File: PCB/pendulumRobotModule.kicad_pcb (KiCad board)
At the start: 2 copper layers, 33 x 100 mm, 26 parts, among them J1 Conn_01x02_Female, J2 conn_3x4, J3 Conn_01x02_Male, J4 Conn_01x04_Female, J5 conn_3x3, J7 Conn_01x04_Female, U1 ESP32-devKit, U2 MPU6050-breakout, U3 buckConverter-adj

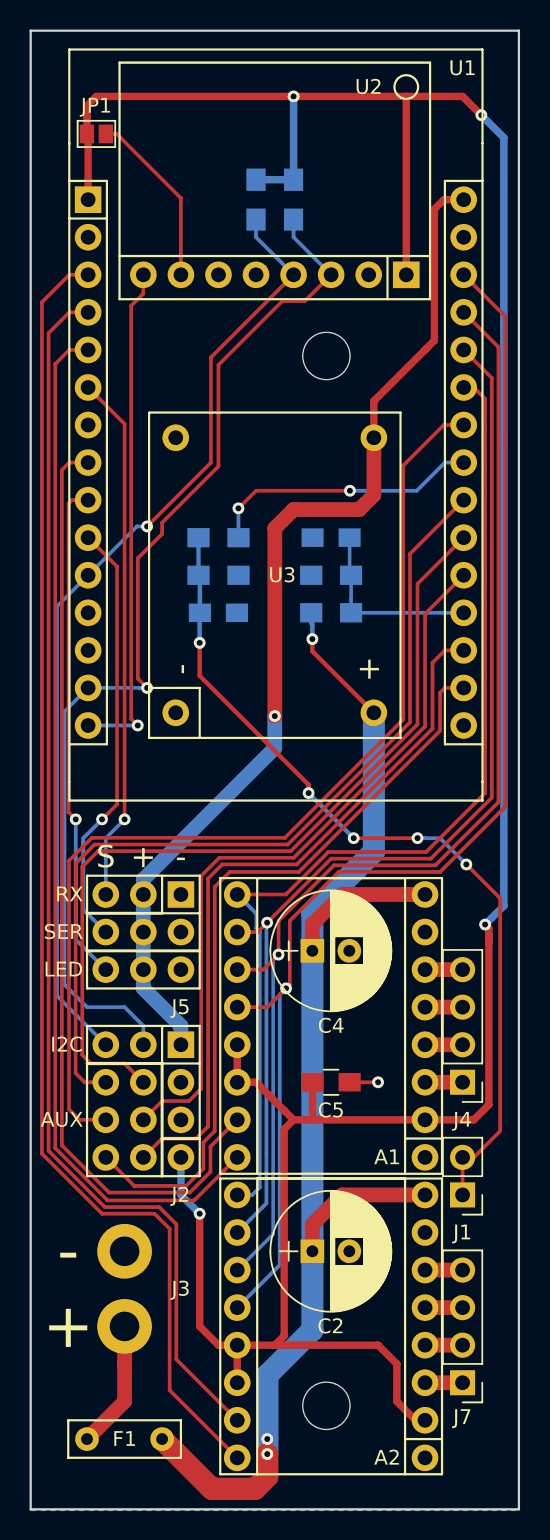
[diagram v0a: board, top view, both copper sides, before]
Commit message: PCB updates: increased 24V trace thickness, added a via (or rather added trace to via) in that signal, and added stepper motor enable pull-up to 3V3.
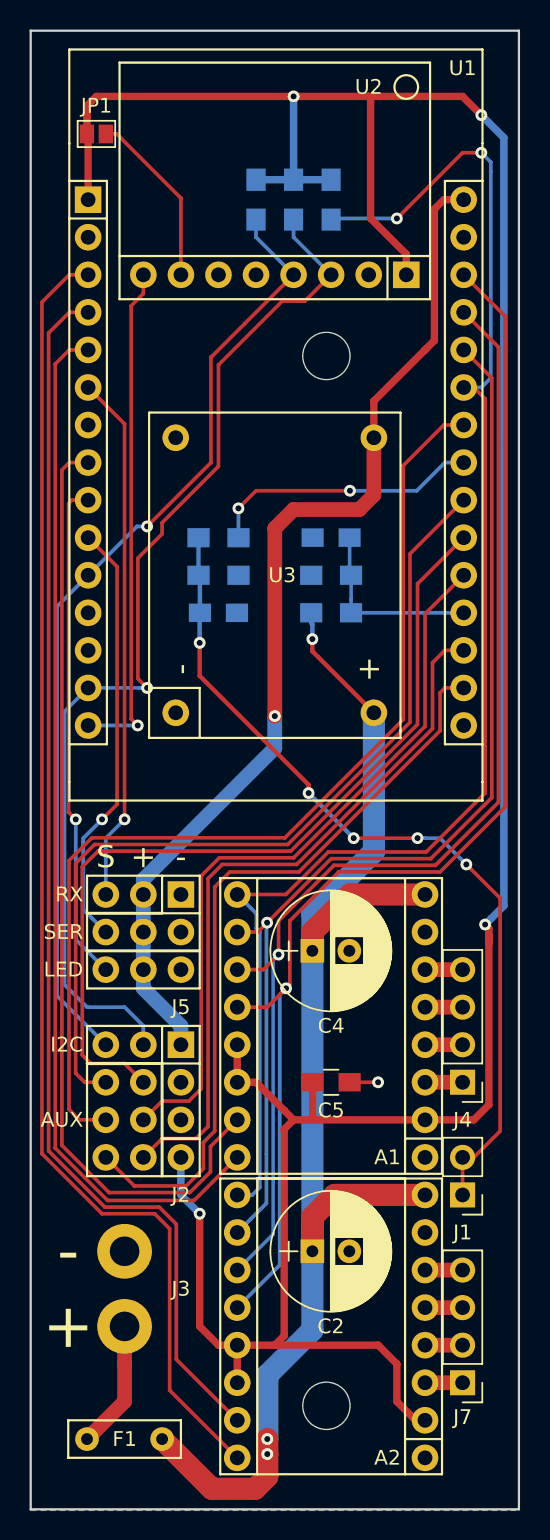
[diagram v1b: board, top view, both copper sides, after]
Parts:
- added R7: 10k, Resistors_SMD:R_0805_HandSoldering, B.Cu at (111.8, 44.5)
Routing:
- net /motEn: track 70.2 -> 99.8 mm, vias 0 -> 2
- net VCC: track 196.1 -> 199.6 mm
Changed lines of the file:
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@@
     (thickness 1.6)
     (drawings 21)
-    (tracks 368)
+    (tracks 383)
     (zones 0)
-    (modules 26)
+    (modules 27)
     (nets 44)
   )
@@
     (tags "resistor 0805")
     (attr smd)
-    (fp_text reference R3 (at 0 2.54) (layer B.SilkS)
+    (fp_text reference R3 (at 3.175 0) (layer B.SilkS)
       (effects (font (size 1 1) (thickness 0.15)) (justify mirror))
     )
@@
     (tags "resistor 0805")
     (attr smd)
-    (fp_text reference R4 (at 0 -2.54) (layer B.SilkS)
+    (fp_text reference R4 (at 3.175 0) (layer B.SilkS)
       (effects (font (size 1 1) (thickness 0.15)) (justify mirror))
     )
@@
     )
   )
+  (module Resistors_SMD:R_0805_HandSoldering (layer B.Cu)
+    (at 111.76 44.45 270)
+    (descr "Resistor SMD 0805, hand soldering")
+    (tags "resistor 0805")
+    (attr smd)
+    (fp_text reference R7 (at -3.175 0 180) (layer B.SilkS)
+      (effects (font (size 1 1) (thickness 0.15)) (justify mirror))
+    )
+    (fp_text value 10k (at 0 -1.75 270) (layer B.Fab)
+      (effects (font (size 1 1) (thickness 0.15)) (justify mirror))
+    )
+    (fp_line (start 2.35 -0.9) (end -2.35 -0.9) (layer B.CrtYd) (width 0.05))
+    (fp_line (start 2.35 -0.9) (end 2.35 0.9) (layer B.CrtYd) (width 0.05))
+    (fp_line (start -2.35 0.9) (end -2.35 -0.9) (layer B.CrtYd) (width 0.05))
+    (fp_line (start -2.35 0.9) (end 2.35 0.9) (layer B.CrtYd) (width 0.05))
+    (fp_line (start -0.6 0.88) (end 0.6 0.88) (layer B.SilkS) (width 0.12))
+    (fp_line (start 0.6 -0.88) (end -0.6 -0.88) (layer B.SilkS) (width 0.12))
+    (fp_line (start -1 0.62) (end 1 0.62) (layer B.Fab) (width 0.1))
+    (fp_line (start 1 0.62) (end 1 -0.62) (layer B.Fab) (width 0.1))
+    (fp_line (start 1 -0.62) (end -1 -0.62) (layer B.Fab) (width 0.1))
+    (fp_line (start -1 -0.62) (end -1 0.62) (layer B.Fab) (width 0.1))
+    (fp_text user %R (at 0 0 270) (layer B.Fab)
+      (effects (font (size 0.5 0.5) (thickness 0.075)) (justify mirror))
+    )
+    (pad 2 smd rect (at 1.35 0 270) (size 1.5 1.3) (layers B.Cu B.Paste B.Mask)
+      (net 33 /motEn))
+    (pad 1 smd rect (at -1.35 0 270) (size 1.5 1.3) (layers B.Cu B.Paste B.Mask)
+      (net 5 VCC))
+    (model ${KISYS3DMOD}/Resistors_SMD.3dshapes/R_0805.wrl
+      (at (xyz 0 0 0))
+      (scale (xyz 1 1 1))
+      (rotate (xyz 0 0 0))
+    )
+  )
   (gr_text "October 2018\ngitlab.com/kloppertje/PendulumRobot/\nelexperiment.nl" (at 107.696 39.37) (layer B.SilkS)
     (effects (font (size 1 1) (thickness 0.2)) (justify mirror))
@@
   (segment (start 123.19 91.694) (end 123.19 107.442) (width 0.25) (layer F.Cu) (net 2))
   (segment (start 110.49 115.57) (end 110.49 95.25) (width 1.5) (layer B.Cu) (net 3))
-  (segment (start 110.49 113.77) (end 110.49 115.57) (width 1) (layer F.Cu) (net 3))
-  (segment (start 112.5 111.76) (end 110.49 113.77) (width 1) (layer F.Cu) (net 3))
-  (segment (start 118.11 111.76) (end 112.5 111.76) (width 1) (layer F.Cu) (net 3))
   (segment (start 110.49 95.25) (end 110.49 92.71) (width 1.5) (layer B.Cu) (net 3))
   (segment (start 110.49 92.71) (end 114.65 88.55) (width 1.5) (layer B.Cu) (net 3))
   (segment (start 114.65 88.55) (end 114.65 79.15) (width 1.5) (layer B.Cu) (net 3))
-  (segment (start 116.837208 91.44) (end 118.11 91.44) (width 1) (layer F.Cu) (net 3))
-  (segment (start 112.5 91.44) (end 116.837208 91.44) (width 1) (layer F.Cu) (net 3))
-  (segment (start 110.49 93.45) (end 112.5 91.44) (width 1) (layer F.Cu) (net 3))
-  (segment (start 110.49 95.25) (end 110.49 93.45) (width 1) (layer F.Cu) (net 3))
   (segment (start 110.41 72.39) (end 110.41 73.072) (width 0.3) (layer B.Cu) (net 3))
   (segment (start 110.41 73.072) (end 110.49 73.152) (width 0.3) (layer B.Cu) (net 3))
@@
   (segment (start 107.442 123.952) (end 110.49 120.904) (width 1.5) (layer B.Cu) (net 3))
   (via (at 107.442 129.286) (size 0.8) (drill 0.4) (layers F.Cu B.Cu) (net 3))
-  (segment (start 107.442 128.27) (end 107.442 129.286) (width 1.5) (layer B.Cu) (net 3))
+  (segment (start 107.442 129.286) (end 107.442 128.27) (width 1.5) (layer F.Cu) (net 3))
+  (segment (start 110.49 113.27) (end 112 111.76) (width 1.5) (layer F.Cu) (net 3))
+  (segment (start 110.49 115.57) (end 110.49 113.27) (width 1.5) (layer F.Cu) (net 3))
+  (segment (start 112 111.76) (end 118.11 111.76) (width 1.5) (layer F.Cu) (net 3))
+  (segment (start 110.49 95.25) (end 110.49 93.98) (width 1.5) (layer F.Cu) (net 3))
+  (segment (start 113.03 91.44) (end 118.11 91.44) (width 1.5) (layer F.Cu) (net 3))
+  (segment (start 110.49 93.98) (end 113.03 91.44) (width 1.5) (layer F.Cu) (net 3))
   (segment (start 113.01 69.75) (end 113.11 69.85) (width 0.25) (layer B.Cu) (net 4))
   (segment (start 113.01 67.31) (end 113.01 69.75) (width 0.25) (layer B.Cu) (net 4))
@@
   (segment (start 121.92 38.735) (end 123.444 40.259) (width 0.5) (layer B.Cu) (net 5))
   (segment (start 123.444 40.259) (end 123.444 92.202) (width 0.5) (layer B.Cu) (net 5))
-  (segment (start 116.84 49.53) (end 116.84 37.465) (width 0.5) (layer F.Cu) (net 5))
   (segment (start 95.885 37.465) (end 109.22 37.465) (width 0.5) (layer F.Cu) (net 5))
   (segment (start 116.84 37.465) (end 120.65 37.465) (width 0.5) (layer F.Cu) (net 5))
   (segment (start 109.22 43.1) (end 106.68 43.1) (width 0.5) (layer B.Cu) (net 5))
-  (segment (start 109.22 37.465) (end 116.84 37.465) (width 0.5) (layer F.Cu) (net 5))
   (via (at 109.22 37.465) (size 0.8) (drill 0.4) (layers F.Cu B.Cu) (net 5))
   (segment (start 109.22 41.83) (end 109.22 37.465) (width 0.5) (layer B.Cu) (net 5))
   (segment (start 109.22 41.83) (end 109.22 43.1) (width 0.5) (layer B.Cu) (net 5))
+  (segment (start 109.22 43.1) (end 111.76 43.1) (width 0.5) (layer B.Cu) (net 5))
+  (segment (start 116.84 48.13) (end 114.43 45.72) (width 0.5) (layer F.Cu) (net 5))
+  (segment (start 116.84 49.53) (end 116.84 48.13) (width 0.5) (layer F.Cu) (net 5))
+  (segment (start 114.43 37.595) (end 114.3 37.465) (width 0.5) (layer F.Cu) (net 5))
+  (segment (start 114.43 45.72) (end 114.43 37.595) (width 0.5) (layer F.Cu) (net 5))
+  (segment (start 109.22 37.465) (end 114.3 37.465) (width 0.5) (layer F.Cu) (net 5))
+  (segment (start 114.3 37.465) (end 116.84 37.465) (width 0.5) (layer F.Cu) (net 5))
   (segment (start 95.325001 64.77) (end 94.234 64.77) (width 0.25) (layer F.Cu) (net 6))
   (segment (start 94.234 64.77) (end 94.00204 65.00196) (width 0.25) (layer F.Cu) (net 6))
@@
   (segment (start 106.704299 93.750299) (end 106.704299 92.734299) (width 0.25) (layer B.Cu) (net 33))
   (segment (start 106.704299 92.734299) (end 106.309999 92.339999) (width 0.25) (layer B.Cu) (net 33))
+  (segment (start 120.725001 57.15) (end 121.92 57.15) (width 0.25) (layer B.Cu) (net 33))
+  (segment (start 121.92 57.15) (end 122.555 56.515) (width 0.25) (layer B.Cu) (net 33))
+  (segment (start 122.555 56.515) (end 122.555 42.545) (width 0.25) (layer B.Cu) (net 33))
+  (segment (start 122.555 42.545) (end 122.555 41.91) (width 0.25) (layer B.Cu) (net 33))
+  (via (at 121.92 41.275) (size 0.8) (drill 0.4) (layers F.Cu B.Cu) (net 33))
+  (segment (start 122.555 41.91) (end 121.92 41.275) (width 0.25) (layer B.Cu) (net 33))
+  (segment (start 121.92 41.275) (end 120.65 41.275) (width 0.25) (layer F.Cu) (net 33))
+  (via (at 116.205 45.72) (size 0.8) (drill 0.4) (layers F.Cu B.Cu) (net 33))
+  (segment (start 120.65 41.275) (end 116.205 45.72) (width 0.25) (layer F.Cu) (net 33))
+  (segment (start 111.84 45.72) (end 111.76 45.8) (width 0.25) (layer B.Cu) (net 33))
+  (segment (start 116.205 45.72) (end 111.84 45.72) (width 0.25) (layer B.Cu) (net 33))
   (via (at 107.95 79.375) (size 0.8) (drill 0.4) (layers F.Cu B.Cu) (net 34))
   (segment (start 107.95 81.534) (end 99.06 90.424) (width 1) (layer B.Cu) (net 34))

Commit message: Changed 10uF cap to 1uF. Also, changed text on bottom layer to point to the correct reposityor.
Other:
- board text added: "October 2018 gitlab.com/kloppertje/BalancingRobot/ elexperiment.nl"
- board text removed: "October 2018 gitlab.com/kloppertje/PendulumRobot/ elexperiment.nl"
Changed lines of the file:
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@@
   (page A4)
   (layers
-    (0 F.Cu signal)
-    (31 B.Cu signal)
+    (0 F.Cu signal hide)
+    (31 B.Cu signal hide)
     (32 B.Adhes user)
     (33 F.Adhes user)
@@
     )
   )
-  (gr_text "October 2018\ngitlab.com/kloppertje/PendulumRobot/\nelexperiment.nl" (at 107.696 39.37) (layer B.SilkS)
+  (gr_text "October 2018\ngitlab.com/kloppertje/BalancingRobot/\nelexperiment.nl" (at 107.696 39.37) (layer B.SilkS)
     (effects (font (size 1 1) (thickness 0.2)) (justify mirror))
   )
